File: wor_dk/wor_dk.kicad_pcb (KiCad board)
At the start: 4 copper layers, 217 x 110.1 mm, 135 parts, among them J101 Conn_01x02, J102 Conn_02x03_Odd_Even, J103 Conn_02x03_Odd_Even, J104 Conn_01x02, J201 SWD, J301 SMA, J302 Conn_02x04_Odd_Even, J303 Conn_02x06_Odd_Even, J401 USB_C_Receptacle_USB2.0_16P, J501 SWD, J502 USB_C_Receptacle_USB2.0_16P, J503 SWD, Q501 BSS84, SW201 SW_Push, SW501 SW_Push, U201 nRF52840, U202 TMUX1112PWR, U203 TMUX1112PWR, U301 Si4467, U401 FT232RL, U501 TLV1117-33, U502 LPC11U35FHI33_501, Y201 32.768kHz, Y202 32MHz, Y301 26MHz, Y501 12MHz

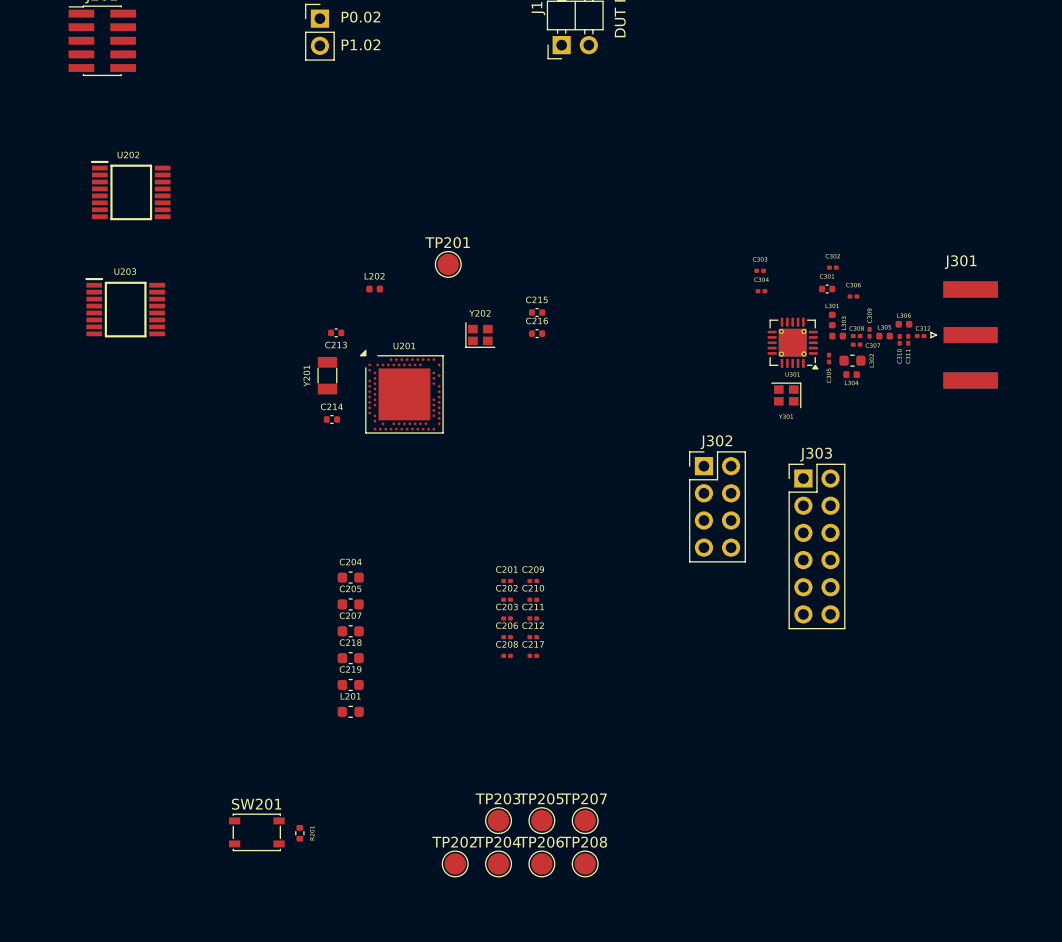
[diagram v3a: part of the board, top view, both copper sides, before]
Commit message: wor_dk: PCB: routing for Si4467
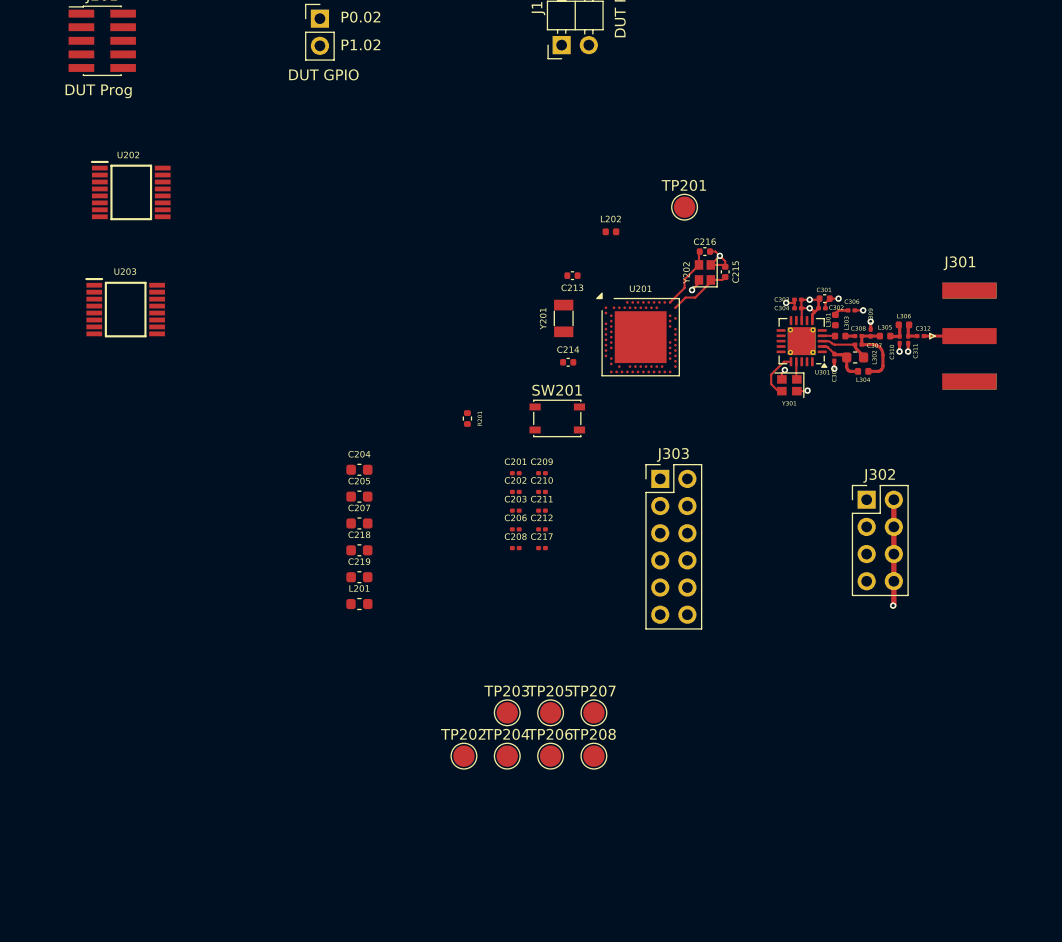
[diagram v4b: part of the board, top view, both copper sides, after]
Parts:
- moved SW201 47.8 mm to (195.0, 91.5)
- moved R201 41.8 mm to (186.6, 91.5)
- moved C214 22.7 mm to (196.0, 86.2)
- moved TP201 22.7 mm to (206.9, 71.8)
- moved U201 22.7 mm to (202.8, 83.9)
- moved Y201 22.7 mm to (195.6, 82.2)
- moved L202 22.7 mm to (200.0, 74.0)
- moved C213 22.7 mm to (196.4, 78.2)
- moved Y202 21.8 mm to (208.8, 77.8), turned to 90 degrees
- moved C215 18.0 mm to (210.7, 77.8), turned to -90 degrees
- moved C216 17.5 mm to (208.8, 75.9), turned to 180 degrees
- moved J302 15.5 mm to (223.9, 99.1)
- moved J303 13.4 mm to (204.6, 97.2)
- moved C207 10.1 mm to (176.5, 101.3)
- moved L201 10.1 mm to (176.5, 108.8)
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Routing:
- net GND: track 60.1 -> 85.5 mm, vias 34 -> 46
- net VDD_DUT: track 0.00 -> 8.85 mm, vias 0 -> 2
- net Net-(C307-Pad2): track 0.00 -> 7.72 mm
- net Net-(U201-XC1): track 0.00 -> 5.96 mm
- net Net-(U201-XC2): track 0.00 -> 5.90 mm
- net Net-(U301-RXp): track 0.00 -> 4.84 mm
- net Net-(U301-RXn): track 0.00 -> 4.61 mm
- net Net-(U301-XOUT): track 0.00 -> 4.52 mm
- net Net-(J301-In): track 0.00 -> 4.39 mm
- net Net-(C310-Pad1): track 0.00 -> 2.13 mm
- net Net-(C311-Pad1): track 0.00 -> 2.08 mm
- net Net-(U301-XIN): track 0.00 -> 1.67 mm
- net Net-(U301-TX): track 0.00 -> 1.20 mm
- net Net-(C308-Pad1): track 0.00 -> 0.90 mm
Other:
- board text added: "DUT GPIO"
- board text added: "DUT Prog"

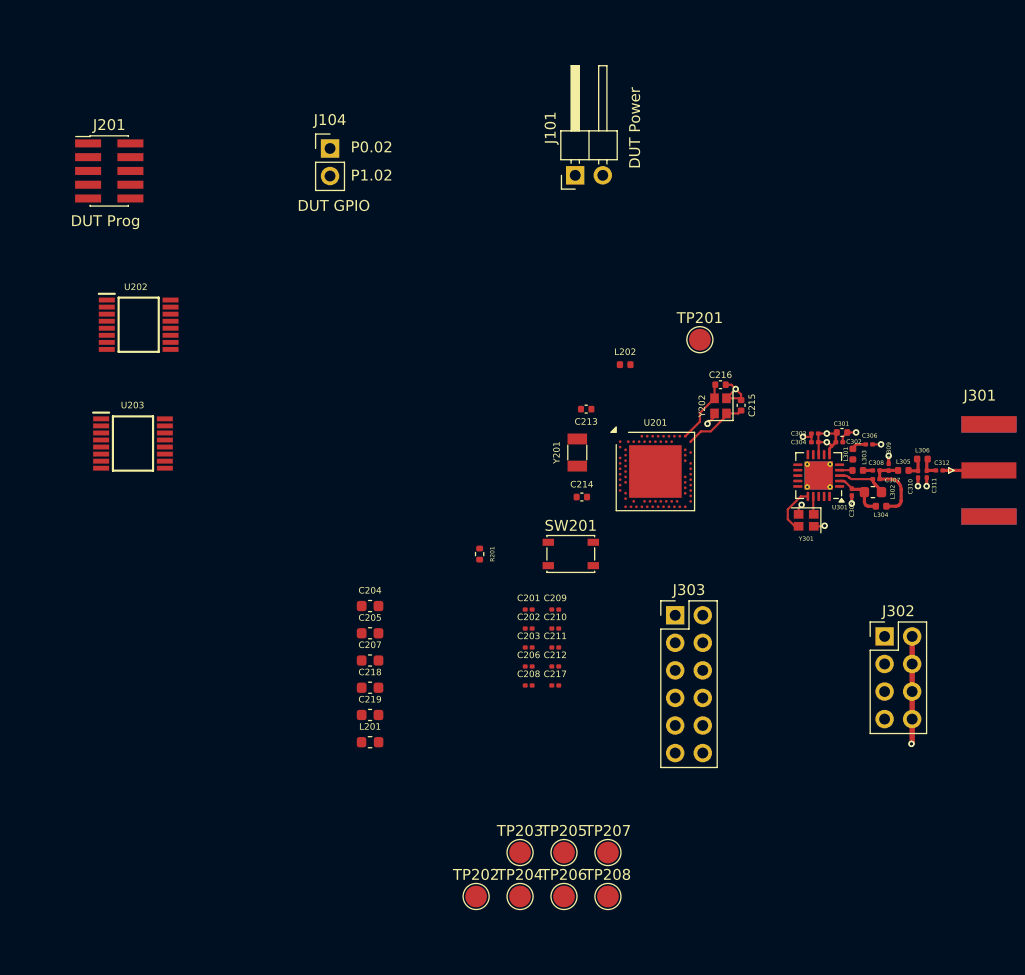
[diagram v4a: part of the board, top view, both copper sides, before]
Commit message: wor_dk: PCB: routing for nRF52840
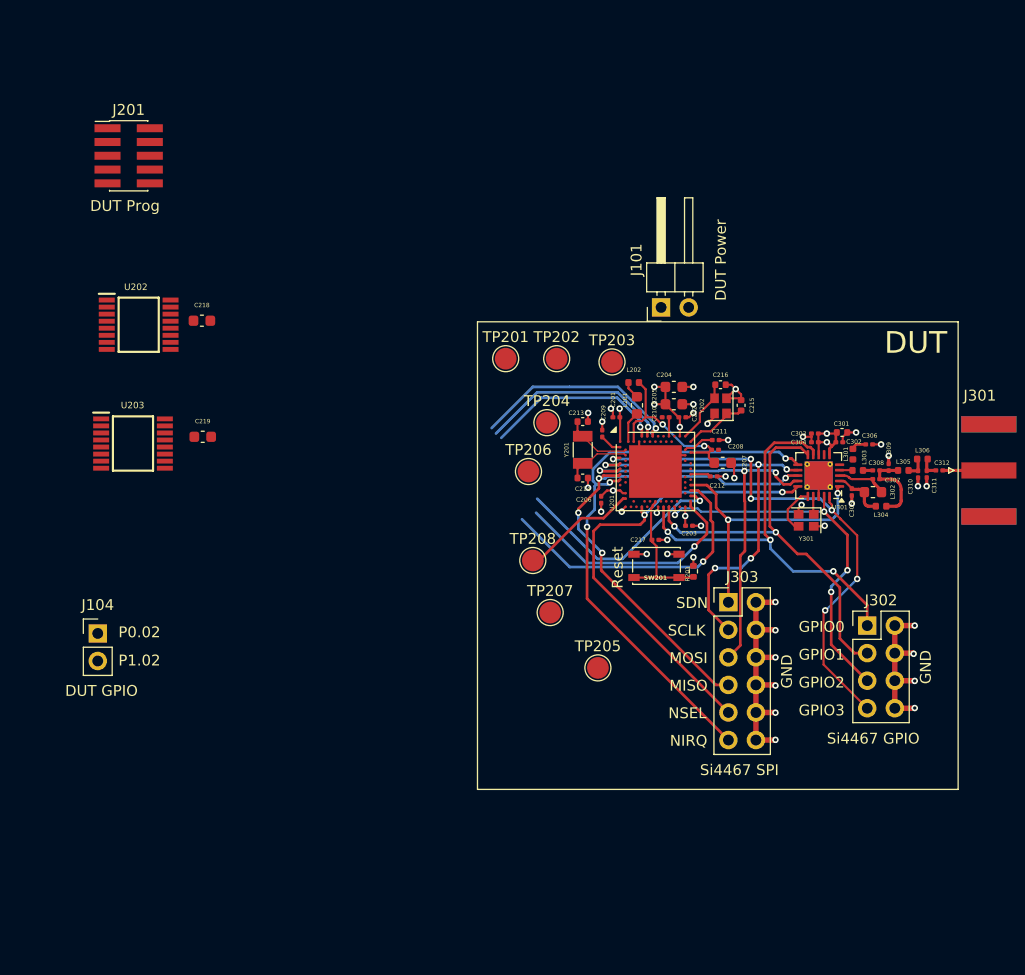
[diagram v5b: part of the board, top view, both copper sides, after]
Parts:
- moved TP202 50.1 mm to (193.7, 73.5)
- moved J104 49.6 mm to (151.4, 98.8)
- moved TP203 46.0 mm to (198.8, 73.8)
- moved TP204 43.7 mm to (192.8, 79.4)
- moved L201 39.6 mm to (201.1, 77.8), turned to 90 degrees
- moved TP206 39.3 mm to (191.1, 83.9)
- moved C207 37.3 mm to (209.0, 83.1)
- moved C218 37.2 mm to (161.0, 70.0)
- moved C205 35.1 mm to (204.5, 77.7)
- moved C204 34.5 mm to (204.5, 76.1)
- moved TP208 31.7 mm to (191.5, 92.1)
- moved C219 29.9 mm to (161.1, 80.7)
- moved C208 27.7 mm to (208.3, 81.9)
- moved C211 24.2 mm to (208.4, 81.0)
- moved C202 24.1 mm to (205.3, 78.9)
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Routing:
- net /Transceiver/NIRQ: track 0.00 -> 53.2 mm, vias 0 -> 3
- net GND: track 85.5 -> 136.9 mm, vias 46 -> 71
- net /Transceiver/GPIO3: track 0.00 -> 48.8 mm, vias 0 -> 6
- net /Transceiver/MISO: track 0.00 -> 47.4 mm, vias 0 -> 4
- net /Transceiver/NSEL: track 0.00 -> 43.5 mm, vias 0 -> 2
- net /Transceiver/GPIO0: track 0.00 -> 39.8 mm, vias 0 -> 3
- net /Transceiver/MOSI: track 0.00 -> 39.0 mm, vias 0 -> 3
- net /Transceiver/GPIO1: track 0.00 -> 38.9 mm, vias 0 -> 2
- net /Transceiver/SCLK: track 0.00 -> 38.7 mm, vias 0 -> 5
- net /Transceiver/GPIO2: track 0.00 -> 34.8 mm, vias 0 -> 4
- net /Main MCU/P1.02_: track 0.00 -> 26.9 mm, vias 0 -> 1
- net /Transceiver/SDN: track 0.00 -> 26.1 mm, vias 0 -> 2
- net /Main MCU/SWDIO_: track 0.00 -> 22.4 mm, vias 0 -> 1
- net /Main MCU/SWCLK_: track 0.00 -> 20.5 mm, vias 0 -> 1
- net /Main MCU/P0.02_: track 0.00 -> 20.4 mm, vias 0 -> 1
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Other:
- board text added: "DUT"
- board text added: "GND"
- board text added: "GPIO0"
- board text added: "GPIO1"
- board text added: "GPIO2"
- board text added: "GPIO3"
- board text added: "MISO"
- board text added: "MOSI"
- board text added: "NIRQ"
- board text added: "NSEL"
- board text added: "Reset"
- board text added: "SCLK"
- board text added: "SDN"
- board text added: "Si4467 GPIO"
- board text added: "Si4467 SPI"

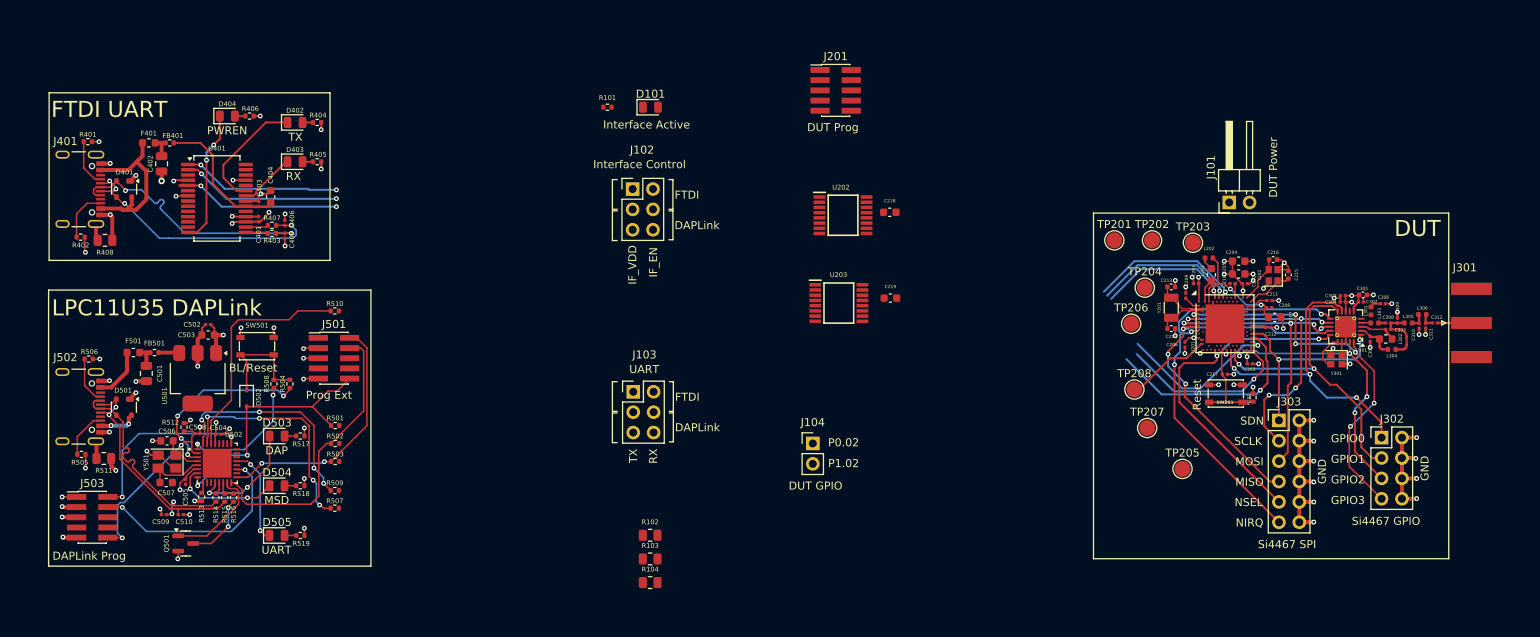
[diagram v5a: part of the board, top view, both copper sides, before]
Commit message: wor_dk: PCB: routing of interface control & switch
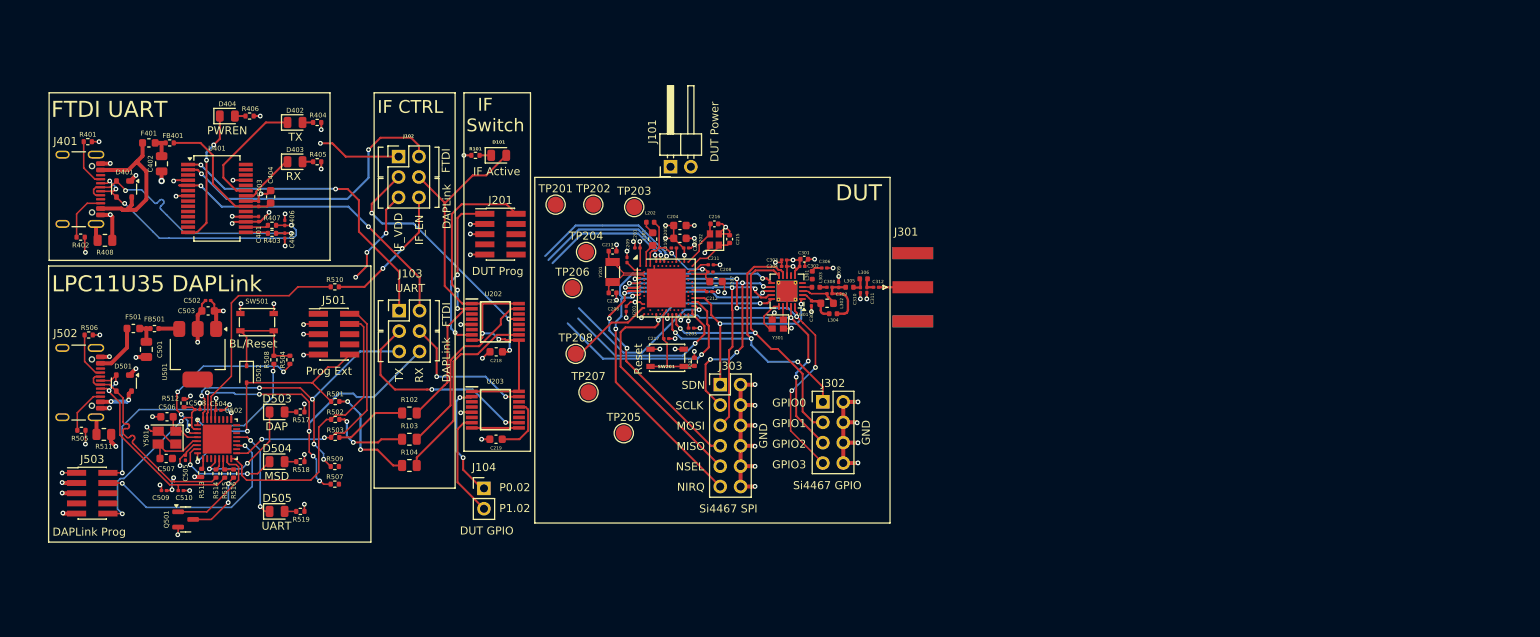
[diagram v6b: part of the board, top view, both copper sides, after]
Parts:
- moved C203 69.8 mm to (136.2, 84.4)
- moved C206 69.8 mm to (128.1, 82.0)
- moved C208 69.8 mm to (138.6, 77.4)
- moved C209 69.8 mm to (128.2, 75.9)
- moved C210 69.8 mm to (134.1, 74.4)
- moved C216 69.8 mm to (139.1, 71.4)
- moved C217 69.8 mm to (133.1, 85.7)
- moved C305 69.8 mm to (151.2, 81.3)
- moved C307 69.8 mm to (153.5, 80.1)
- moved C308 69.8 mm to (153.5, 79.3)
- moved C309 69.8 mm to (154.6, 79.0)
- moved C312 69.8 mm to (159.3, 79.3)
- moved J303 69.8 mm to (139.9, 91.5)
- moved L202 69.8 mm to (131.1, 71.2)
- moved L305 69.8 mm to (156.0, 79.3)
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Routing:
- net /IF_EN: track 0.00 -> 64.0 mm, vias 0 -> 2
- net /VDD_AUX: track 0.00 -> 42.2 mm, vias 0 -> 3
- net /Main MCU/SWDIO: track 0.00 -> 39.2 mm, vias 0 -> 2
- net /RXD_DUT: track 0.00 -> 26.2 mm, vias 0 -> 2
- net /Main MCU/NRESET: track 0.00 -> 24.4 mm
- net /Main MCU/SWCLK: track 0.00 -> 23.2 mm
- net /Main MCU/VDD_DUT_OUT: track 0.00 -> 20.7 mm, vias 0 -> 2
- net /TXD_FTDI: track 19.8 -> 39.0 mm
- net /RXD_DAP: track 28.5 -> 47.4 mm, vias 4 -> 5
- net /RXD_FTDI: track 21.8 -> 39.9 mm
- net /TXD_DUT: track 0.00 -> 17.9 mm, vias 0 -> 2
- net /DTR_FTDI: track 20.0 -> 37.3 mm
- net /DTR_DAP: track 28.8 -> 46.0 mm, vias 0 -> 2
- net /P0.02: track 0.00 -> 14.6 mm, vias 0 -> 2
- net /NRESET: track 0.00 -> 13.8 mm, vias 0 -> 2
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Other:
- board text added: "IF Active"
- board text added: "IF CTRL"
- board text added: "IF Switch"
- board text removed: "Interface Active"
- board text removed: "Interface Control"

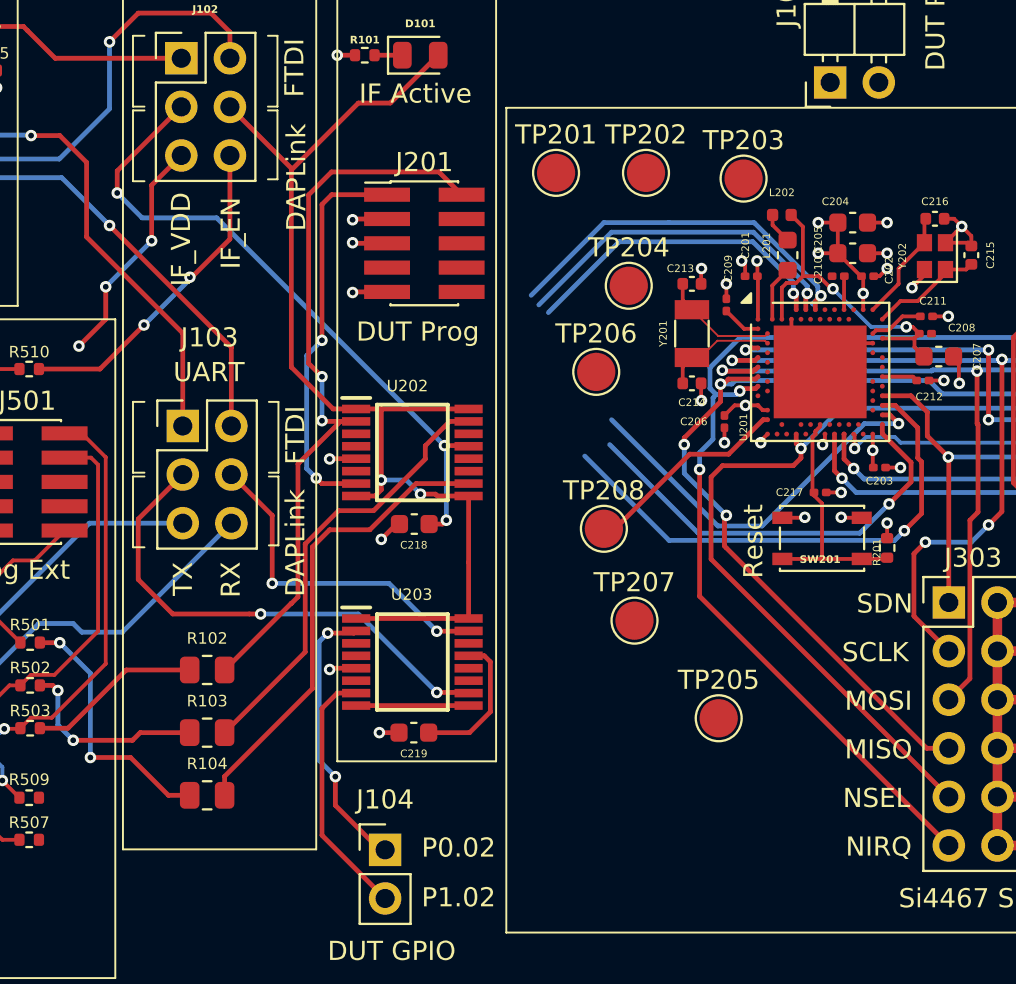
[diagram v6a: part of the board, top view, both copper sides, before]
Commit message: wor_dk: PCB: routing of IF switch part
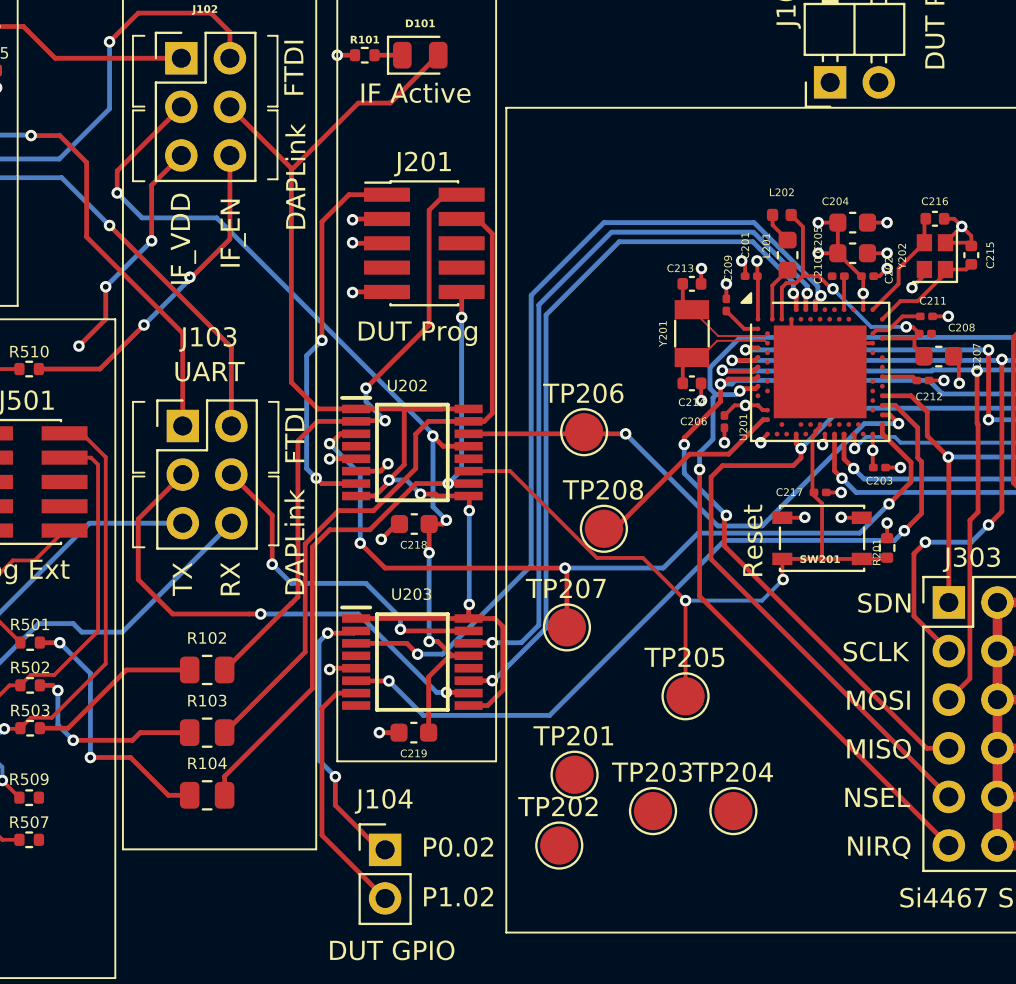
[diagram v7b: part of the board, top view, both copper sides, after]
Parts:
- moved TP202 35.4 mm to (119.5, 104.2)
- moved TP203 33.4 mm to (124.4, 102.4)
- moved TP201 31.5 mm to (120.3, 100.5)
- moved TP204 28.0 mm to (128.6, 102.4)
- moved TP207 3.55 mm to (119.9, 92.8)
- moved TP206 3.21 mm to (120.8, 82.6)
- moved TP205 2.08 mm to (126.1, 96.4)
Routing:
- net /Main MCU/NRESET_: track 12.9 -> 38.7 mm, vias 0 -> 2
- net /Main MCU/P0.02_: track 20.4 -> 45.1 mm, vias 1 -> 2
- net /Main MCU/SWDIO_: track 22.4 -> 45.4 mm, vias 1 -> 4
- net VDD_DUT: track 24.8 -> 46.6 mm, vias 10 -> 11
- net /Main MCU/P0.31_: track 16.7 -> 38.4 mm, vias 1 -> 2
- net /Main MCU/P0.29_: track 18.0 -> 38.8 mm, vias 1 -> 2
- net /Main MCU/P1.02_: track 26.9 -> 41.6 mm, vias 1 -> 2
- net /Main MCU/SWCLK: track 23.2 -> 36.6 mm
- net /Main MCU/NRESET: track 24.4 -> 35.8 mm, vias 0 -> 2
- net /Main MCU/SWCLK_: track 20.5 -> 27.7 mm, vias 1 -> 2
- net /VDD_AUX: track 42.2 -> 48.6 mm, vias 3 -> 5
- net /Main MCU/SWDIO: track 39.2 -> 33.4 mm
- net /IF_EN: track 64.0 -> 68.1 mm, vias 2 -> 4
- net /Main MCU/VDD_DUT_OUT: track 20.7 -> 20.1 mm
